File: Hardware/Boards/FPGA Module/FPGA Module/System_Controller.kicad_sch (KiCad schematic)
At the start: 25 parts, among them SW1 RST, U5 W25Q16JVUXIQ TR, U6 RP2040, Y1 12Mhz

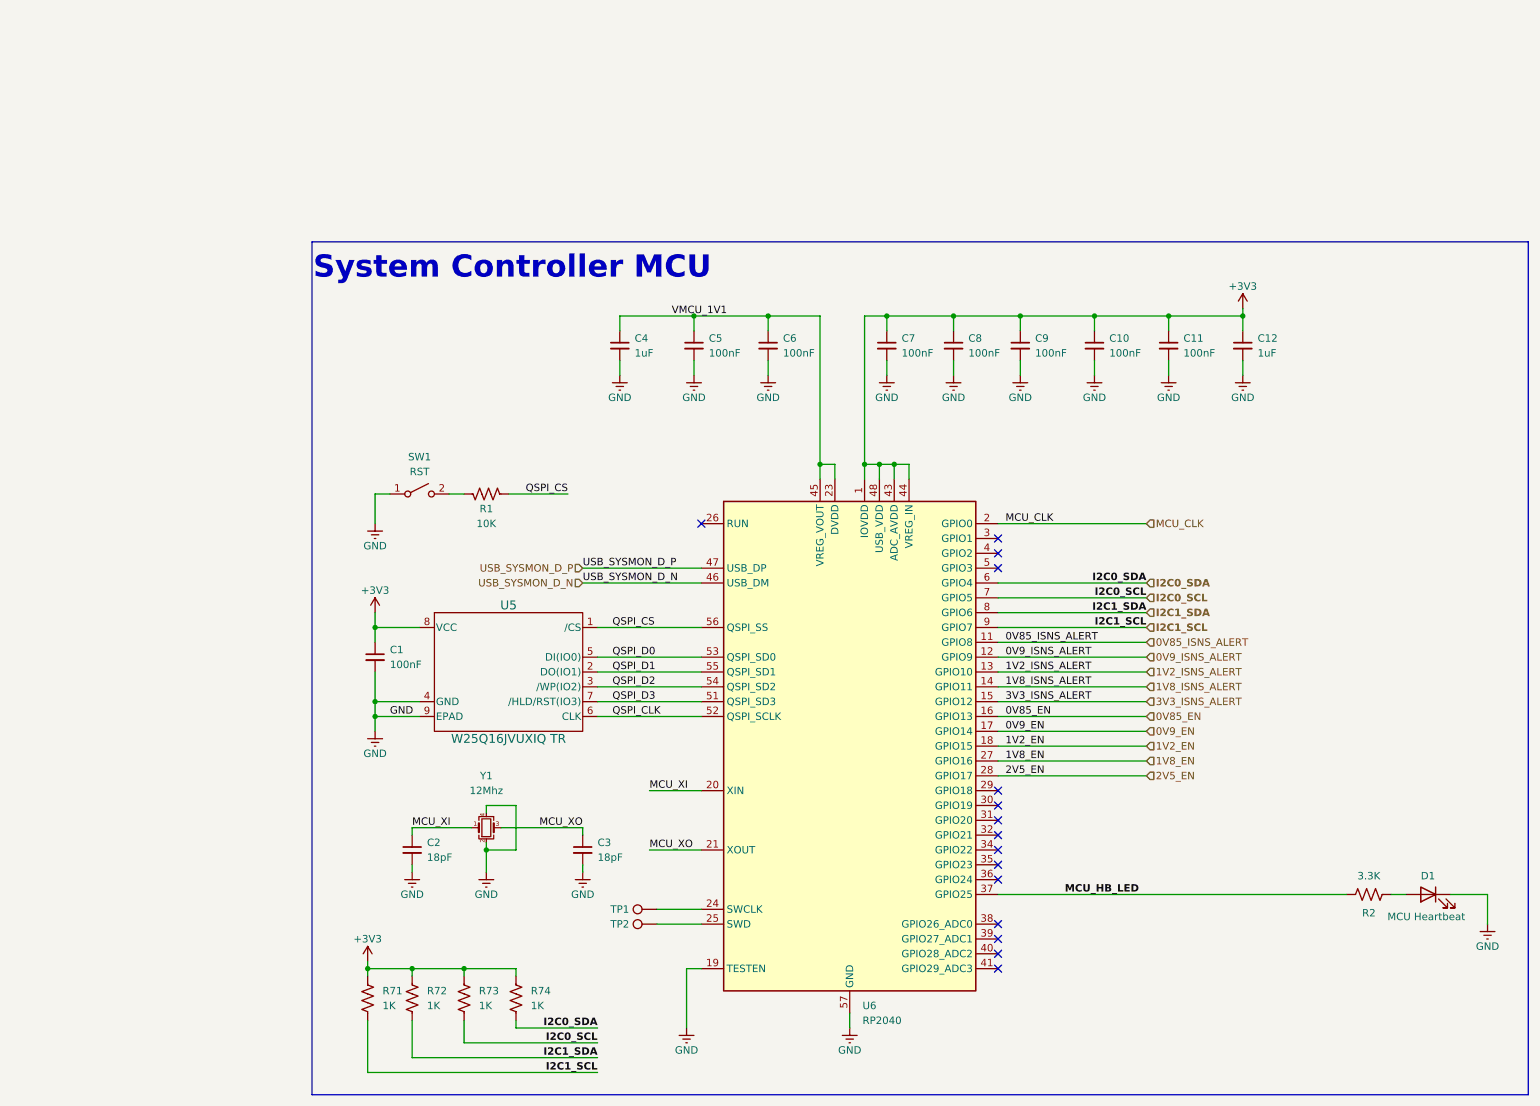
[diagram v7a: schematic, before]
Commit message: FPGA Module sch update
Added 3V3 LDO for MCU and 3V3 EN for DCDC. Also added SPI bus from MCU to FPGA with level shifter
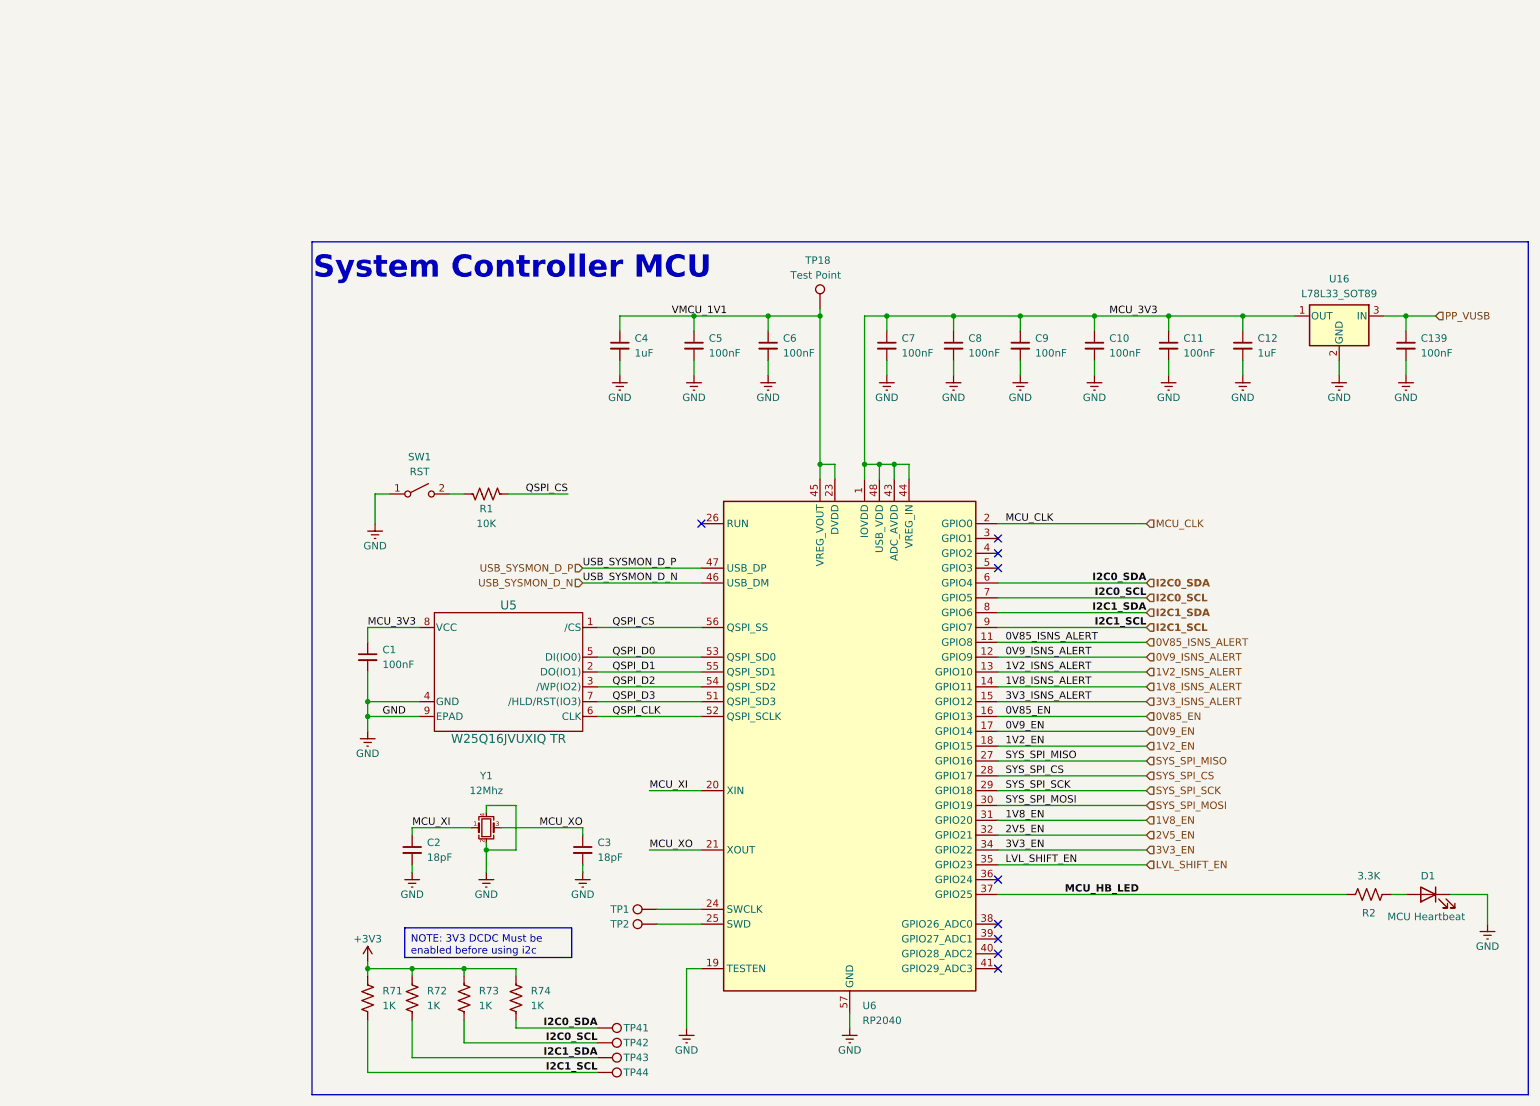
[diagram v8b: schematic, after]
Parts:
- added C139: 100nF, Capacitor_SMD:C_0201_0603Metric, symbol Device:C_Small
- added TP18, TP41, TP42, TP43, TP44: Test Point, FPGA Module:Test Point 0.75mm, symbol Connector:TestPoint
- added U16: L78L33_SOT89, Package_TO_SOT_SMD:SOT-89-3, symbol Regulator_Linear:L78L33_SOT89
- TP1, TP2: footprint TestPoint:TestPoint_Pad_D1.0mm -> FPGA Module:Test Point 0.75mm
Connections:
- net +3V3: no longer C1.1, C10.1, C11.1, C12.1, C7.1, C8.1, C9.1, U5.8 (VCC), U6.1 (IOVDD), U6.10 (IOVDD), U6.22 (IOVDD), U6.33 (IOVDD), U6.42 (IOVDD), U6.43 (ADC_AVDD), U6.44 (VREG_IN), U6.48 (USB_VDD), U6.49 (IOVDD)
- net 1V8_EN: now also U6.31 (GPIO20); no longer U6.27 (GPIO16)
- net 2V5_EN: now also U6.32 (GPIO21); no longer U6.28 (GPIO17)
- net GND: now also C139.2, U16.2 (GND)
- net I2C0_SCL: now also TP42.1
- net I2C0_SDA: now also TP41.1
- net I2C1_SCL: now also TP44.1
- net I2C1_SDA: now also TP43.1
- net VMCU_1V1: now also TP18.1
- net SYS_SPI_SCK: now reaches U6.29 (GPIO18)
- net SYS_SPI_MOSI: now reaches U6.30 (GPIO19)
- net 3V3_EN: now reaches U6.34 (GPIO22)
- net LVL_SHIFT_EN: now reaches U6.35 (GPIO23)
- new net MCU_3V3: C1.1, C10.1, C11.1, C12.1, C7.1, C8.1, C9.1, U16.1 (OUT), U5.8 (VCC), U6.1 (IOVDD), U6.10 (IOVDD), U6.22 (IOVDD), U6.33 (IOVDD), U6.42 (IOVDD), U6.43 (ADC_AVDD), U6.44 (VREG_IN), U6.48 (USB_VDD), U6.49 (IOVDD)
- new net PP_VUSB: C139.1, U16.3 (IN)
- new net SYS_SPI_CS: U6.28 (GPIO17)
- new net SYS_SPI_MISO: U6.27 (GPIO16)
- no-connect marks 15 -> 9
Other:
- moved on the sheet: C1
